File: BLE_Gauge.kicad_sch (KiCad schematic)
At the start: 31 parts, among them J1 TagConnect_TC2030-NL, J2 USB_C_Receptacle_PowerOnly_6P, U1 nRF54L15-QFXX, U2 LSM6DS3, X1 32MHz, X2 32.768kHz

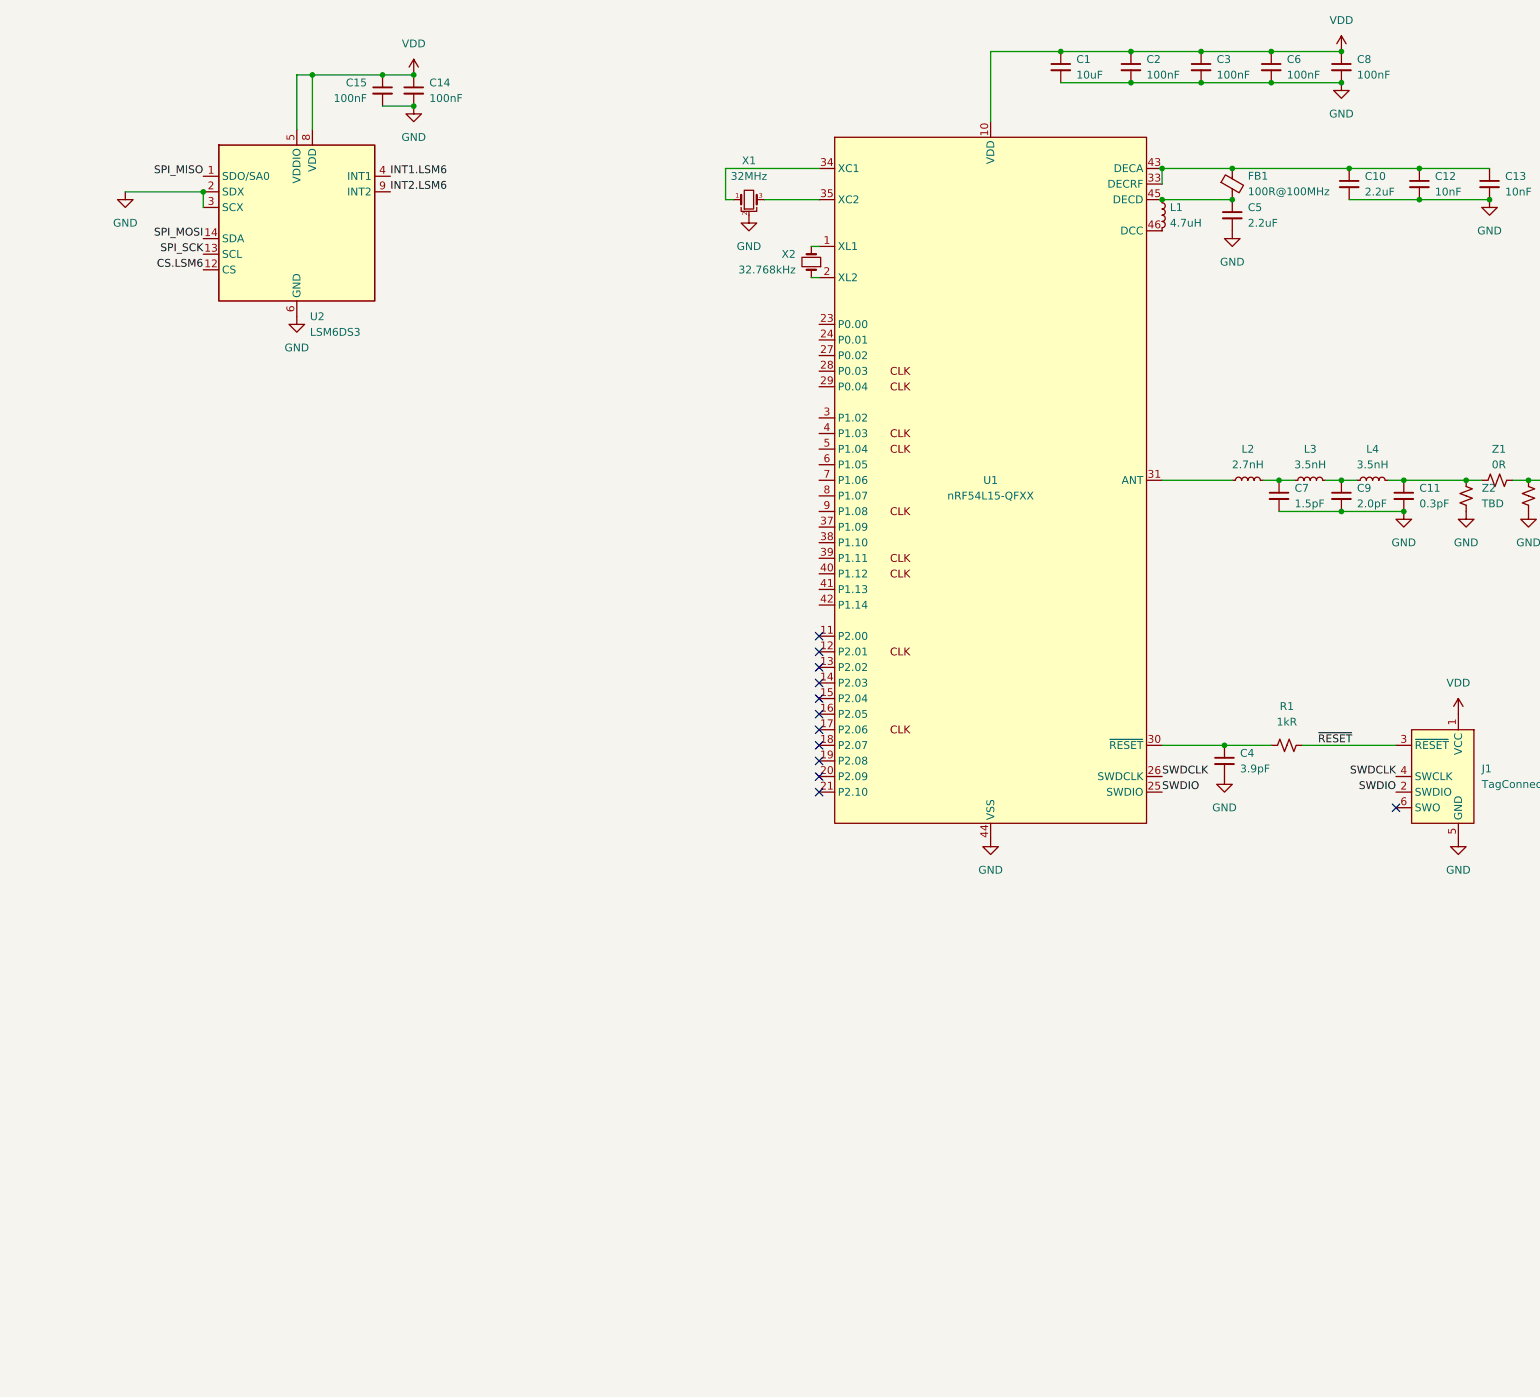
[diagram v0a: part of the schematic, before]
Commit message: Add Display
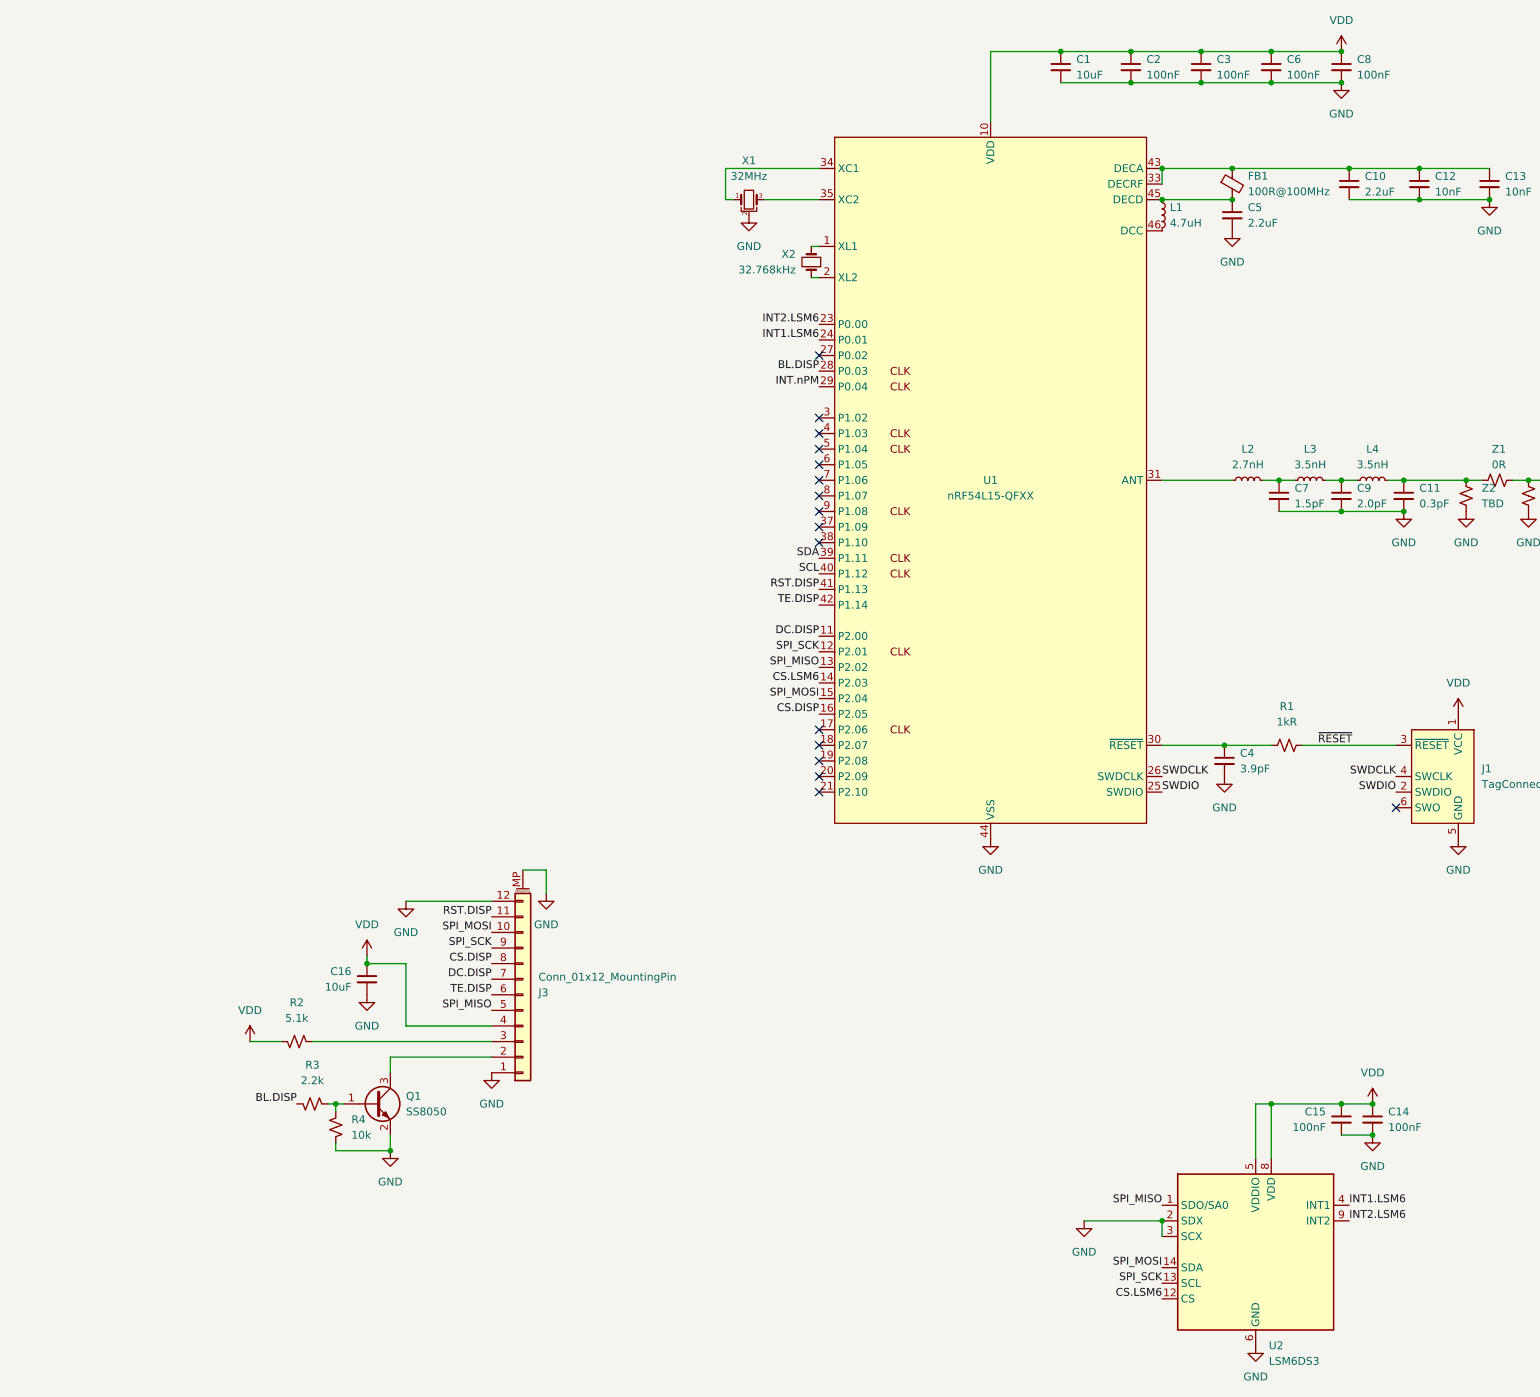
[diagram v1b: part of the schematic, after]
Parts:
- added C16: 10uF, Capacitor_SMD:C_0402_1005Metric, symbol Device:C_Small
- added J3: Conn_01x12_MountingPin, Connector_FFC-FPC:Hirose_FH12-12S-0.5SH_1x12-1MP_P0.50mm_Horizontal, symbol Connector_Generic_MountingPin:Conn_01x12_MountingPin
- added Q1: SS8050, Package_TO_SOT_SMD:SOT-23, symbol Transistor_BJT:SS8050
- added R2: 5.1k, Resistor_SMD:R_0201_0603Metric, symbol Device:R_Small_US
- added R3: 2.2k, Resistor_SMD:R_0201_0603Metric, symbol Device:R_Small_US
- added R4: 10k, Resistor_SMD:R_0201_0603Metric, symbol Device:R_Small_US
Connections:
- net CS.LSM6: now also U1.14 (P2.03)
- net GND: now also C16.2, J3.1 (Pin_1), J3.12 (Pin_12), J3.MP (MountPin), Q1.2 (E), R4.2
- net INT1.LSM6: now also U1.24 (P0.01)
- net INT2.LSM6: now also U1.23 (P0.00)
- net SPI_MISO: now also U1.13 (P2.02), J3.5 (Pin_5)
- net SPI_MOSI: now also U1.15 (P2.04), J3.10 (Pin_10)
- net SPI_SCK: now also U1.12 (P2.01), J3.9 (Pin_9)
- net VDD: now also C16.1, J3.4 (Pin_4), R2.2
- net DC.DISP: now reaches U1.11 (P2.00)
- net DC.DISP: now also J3.7 (Pin_7)
- net CS.DISP: now reaches U1.16 (P2.05)
- net CS.DISP: now also J3.8 (Pin_8)
- net BL.DISP: now reaches U1.28 (P0.03)
- net BL.DISP: now also R3.2
- net INT.nPM: now reaches U1.29 (P0.04)
- net SDA: now reaches U1.39 (P1.11)
- net SCL: now reaches U1.40 (P1.12)
- net RST.DISP: now reaches U1.41 (P1.13)
- net RST.DISP: now also J3.11 (Pin_11)
- net TE.DISP: now reaches U1.42 (P1.14)
- net TE.DISP: now also J3.6 (Pin_6)
- new net: Q1.1 (B), R3.1, R4.1
- new net: J3.2 (Pin_2), Q1.3 (C)
- new net: J3.3 (Pin_3), R2.1
- no-connect marks 12 -> 16
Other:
- moved on the sheet: C14, C15, U2

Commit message: Arrumando bagunça
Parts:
- removed X1: 32MHz, Crystal:Crystal_SMD_2016-4Pin_2.0x1.6mm, symbol Device:Crystal_GND2_Small
- added X1: 32MHz, Crystal:Crystal_SMD_2016-4Pin_2.0x1.6mm, symbol Device:Crystal_GND24_Small
- C1: footprint Capacitor_SMD:C_0402_1005Metric -> Nath:C_0402_1005Metric_Nordic
- C10, C11, C12, C13, C2, C3, C6, C7, C8, C9: footprint Capacitor_SMD:C_0201_0603Metric -> Nath:C_0201_0603Metric_Nordic
- C4: renamed from C5; footprint Capacitor_SMD:C_0201_0603Metric -> Nath:C_0201_0603Metric_Nordic
- C5: renamed from C4; footprint Capacitor_SMD:C_0201_0603Metric -> Nath:C_0201_0603Metric_Nordic
- FB1: value 100R@100MHz -> 120R/0.2A; footprint Inductor_SMD:L_0201_0603Metric -> Nath:L_0201_0603Metric_Nordic
- L1: footprint Inductor_SMD:L_0603_1608Metric -> Nath:L_0603_1608Metric_Nordic
- L2, L3, L4: footprint Inductor_SMD:L_0201_0603Metric -> Nath:L_0201_0603Metric_Nordic
- R1: footprint Resistor_SMD:R_0201_0603Metric -> Nath:R_0201_0603Metric_Nordic
- U1: KiLib_Generator (none) -> package/no_lead
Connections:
- net GND: now also X1.2 (G), X1.4 (G)
- net VDD: no longer C1.1, C2.1, C3.1, C6.1, C8.1, U1.10 (VDD), U1.22 (VDD), U1.36 (VDD), U1.47 (VDD), U1.48 (VDD)
- net RF: now reaches C11.1, L4.2, Z1.2, Z2.2
- net at U1.34 (XC1): now also X1.1
- net at U1.35 (XC2): now also X1.3
- new net VDD_NRF: C1.1, C2.1, C3.1, C6.1, C8.1, U1.10 (VDD), U1.22 (VDD), U1.36 (VDD), U1.47 (VDD), U1.48 (VDD)
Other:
- note added: "Display"
- note added: "IMU"
- note added: "Possivelmente invertido"
- moved on the sheet: AE1, C1, C10, C11, C12, C13, C14, C15, C16, C2, C3, C4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

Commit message: Add PMIC
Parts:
- added C17, C22: 1uF, Nath:C_0603_1608Metric_Nordic, symbol Device:C_Small
- added C18: 100nF, Nath:C_0201_0603Metric_Nordic, symbol Device:C_Small
- added C19, C20, C21, C28: 10uF, Nath:C_0603_1608Metric_Nordic, symbol Device:C_Small
- added C24: 2.2uF, Nath:C_0603_1608Metric_Nordic, symbol Device:C_Small
- added D1: LED_ARGB, symbol Device:LED_ARGB
- added F1: 0.5A, Fuse:Fuse_0603_1608Metric, symbol Device:Polyfuse
- added L6: 2.2uH, Nath:L_0806_2016Metric_Nordic, symbol Device:L_Small
- added R6, R8: 4.7kR, Nath:R_0201_0603Metric_Nordic, symbol Device:R_Small_US
- added R7: 250kR, Nath:R_0201_0603Metric_Nordic, symbol Device:R_Small_US
- added U3: nPM1300-QEAA, Nath:Nordic_QFN50P500X500X90-33N, symbol PCM_nordic-lib-kicad-npm:nPM1300-QEXX
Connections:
- net VDD_NRF is gone; now on net +3V3: C1.1, C2.1, C3.1, C6.1, C8.1, U1.10 (VDD), U1.22 (VDD), U1.36 (VDD), U1.47 (VDD), U1.48 (VDD)
- net GND: now also C17.2, C18.2, C19.2, C20.2, C21.2, C22.2, C24.2, C28.2, R7.2, U3.33 (AVSS), U3.6 (PVSS2)
- net INT.nPM: now also U3.7 (GPIO0)
- net SCL: now also R6.2, U3.14 (SCL)
- net SDA: now also R8.2, U3.13 (SDA)
- net CC1: now reaches J2.A5 (CC1)
- net CC1: now also U3.23 (CC1)
- net at J2.A9 (VBUS), J2.B9 (VBUS): now also F1.1
- net CC2: now reaches J2.B5 (CC2)
- net CC2: now also U3.24 (CC2)
- net VDD renamed +3V3
- net +3V3: now also C28.1, L6.1, R6.1, R8.1, U3.32 (VOUT2)
- new net: D1.2 (RK), U3.25 (LED0)
- new net: D1.3 (GK), U3.26 (LED1)
- new net: D1.4 (BK), U3.27 (LED2)
- new net: C22.1, U3.22 (VBUSOUT)
- new net NTC: U3.18 (NTC)
- new net SHPHLD: U3.15 (SHPHLD)
- new net SW2: L6.2, U3.5 (SW2)
- new net VBAT: C24.1, U3.19 (VBAT)
- new net VBUS: C17.1, F1.2, U3.21 (VBUS)
- new net VDDIO: C18.1, U3.12 (VDDIO)
- new net VSET2: R7.1, U3.16 (VSET2)
- new net VSYS: C19.1, C20.1, C21.1, D1.1 (A), U3.20 (VSYS), U3.4 (PVDD)
- no-connect marks 16 -> 29
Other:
- note added: "3.3V"
- note added: "3.3V 250kR...500kR"
- moved on the sheet: J2

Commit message: Arrumando Bagunça 2
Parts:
- U3: footprint Nath:Nordic_QFN50P500X500X90-33N -> Package_DFN_QFN:QFN-32-1EP_5x5mm_P0.5mm_EP3.6x3.6mm_ThermalVias
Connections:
- net LED0: now reaches D1.2 (RK), U3.25 (LED0)
- net LED1: now reaches D1.3 (GK), U3.26 (LED1)
- net LED2: now reaches D1.4 (BK), U3.27 (LED2)
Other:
- note removed: "3.3V 250kR...500kR"
- moved on the sheet: C17
